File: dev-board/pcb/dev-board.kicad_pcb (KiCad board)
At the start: 2 copper layers, 65 x 56 mm, 82 parts, among them J1 Raspberry_Pi_2_3, J2 USB_B_Micro, Q1 BSS84, Q2 BSS84, U1 MCP2210-I-SS, U10 25LCxxx, U11 25LCxxx, U12 25LCxxx, U13 25LCxxx, U14 25LCxxx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

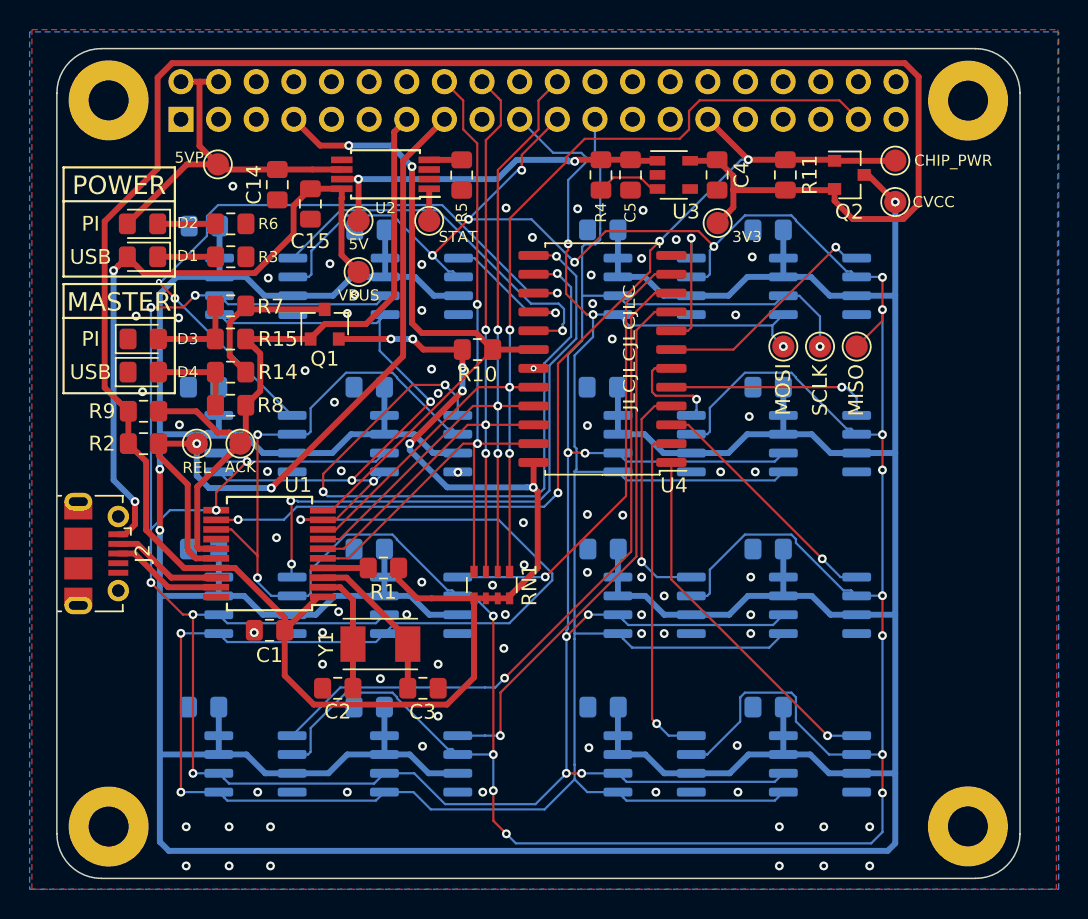
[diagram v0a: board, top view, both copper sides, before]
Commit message: Replace RN1 with 4 0804 resistors
Closes #9
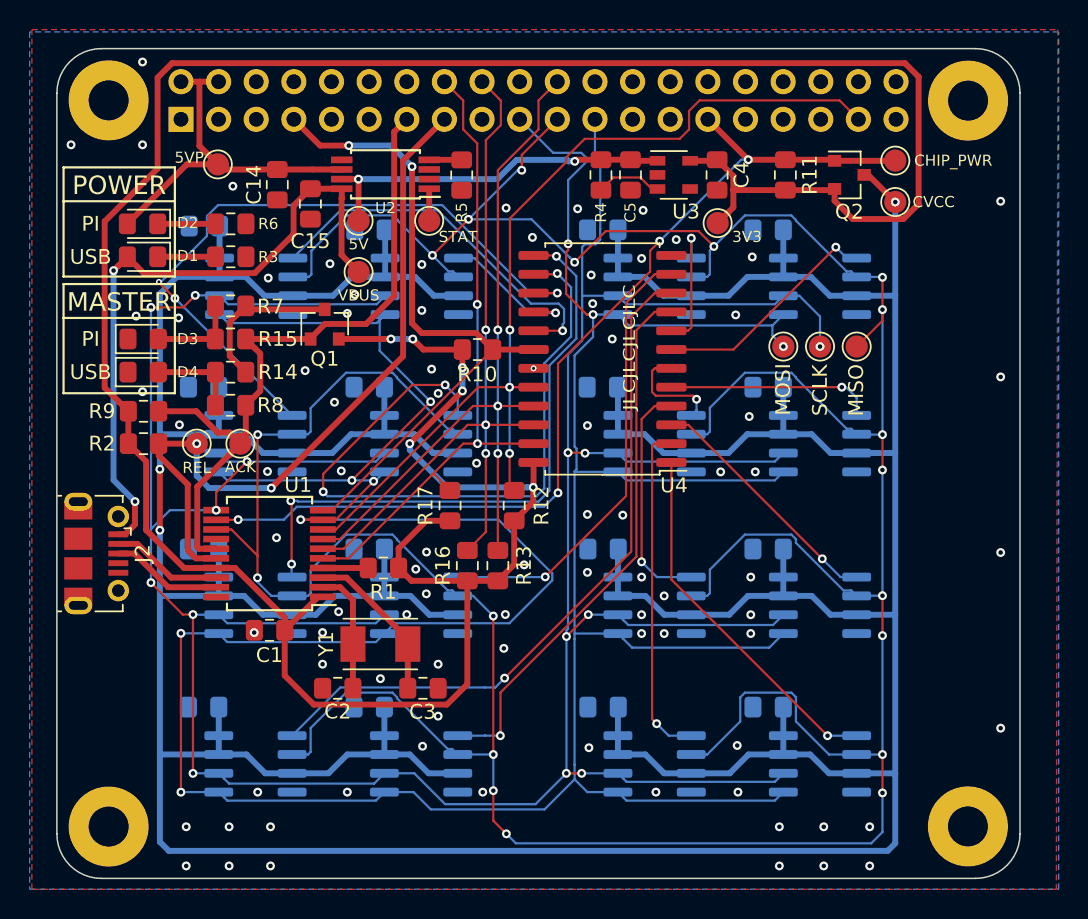
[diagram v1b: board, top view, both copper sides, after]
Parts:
- removed RN1: 10k, Resistor_SMD:R_Array_Convex_4x0603
- added R12: 10k, Capacitor_SMD:C_0805_2012Metric_Pad1.15x1.40mm_HandSolder, F.Cu at (109.4, 91.7)
- added R13: 10k, Capacitor_SMD:C_0805_2012Metric_Pad1.15x1.40mm_HandSolder, F.Cu at (108.3, 95.7)
- added R16: 10k, Capacitor_SMD:C_0805_2012Metric_Pad1.15x1.40mm_HandSolder, F.Cu at (106.2, 95.7)
- added R17: 10k, Capacitor_SMD:C_0805_2012Metric_Pad1.15x1.40mm_HandSolder, F.Cu at (105.1, 91.7)
- R1: value 10K -> 10k
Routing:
- net /CSBIT0: track 51.4 -> 44.4 mm
- net /CSBIT3: track 70.3 -> 65.0 mm
- net +3V3: track 199.3 -> 203.3 mm
- net /CSBIT2: track 52.7 -> 51.2 mm
- net /CSBIT1: track 51.7 -> 50.8 mm
- net GND: vias 80 -> 87
